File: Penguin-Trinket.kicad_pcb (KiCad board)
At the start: 2 copper layers, 66.3 x 76.5 mm, 17 parts, among them M1 Motor_DC, Q1 NPN, Q2 NPN, Q3 NPN, SW1 SW_Push

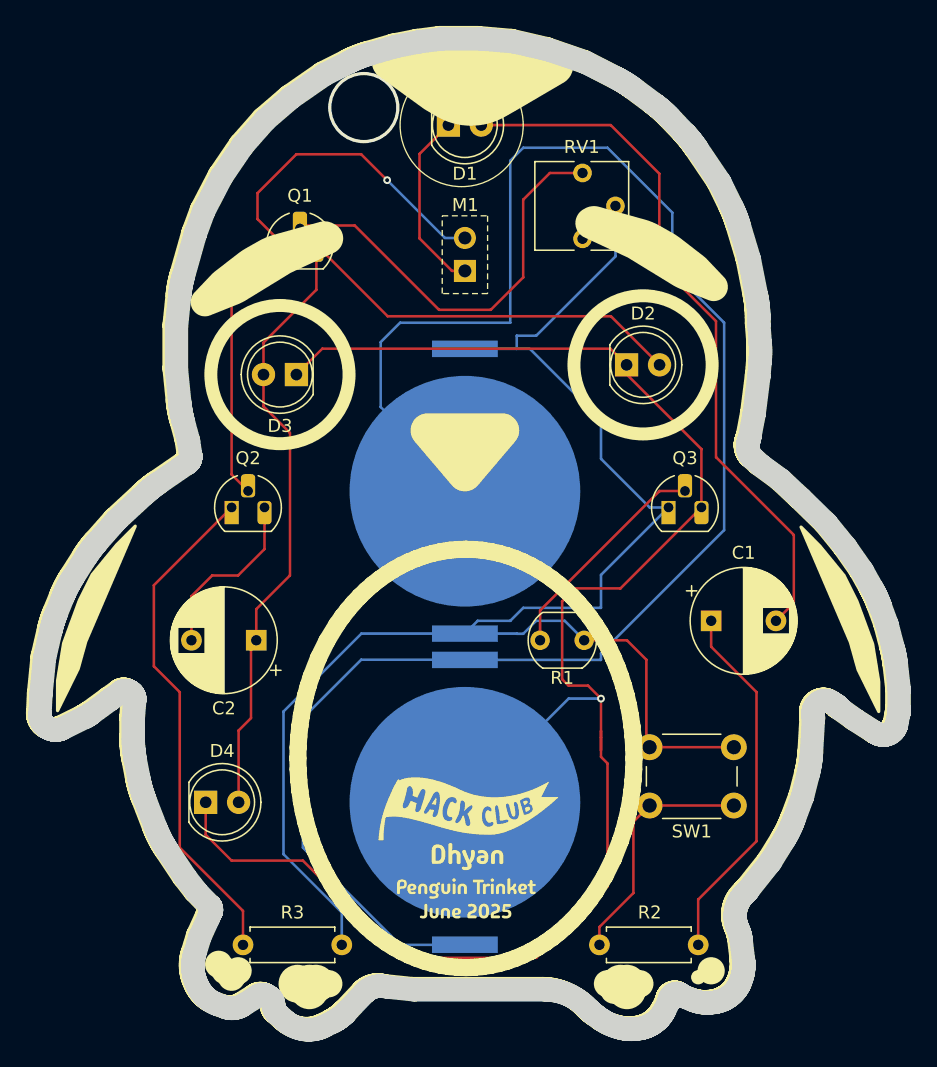
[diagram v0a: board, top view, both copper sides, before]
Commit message: redo (trinket v3)
hopefully everything works
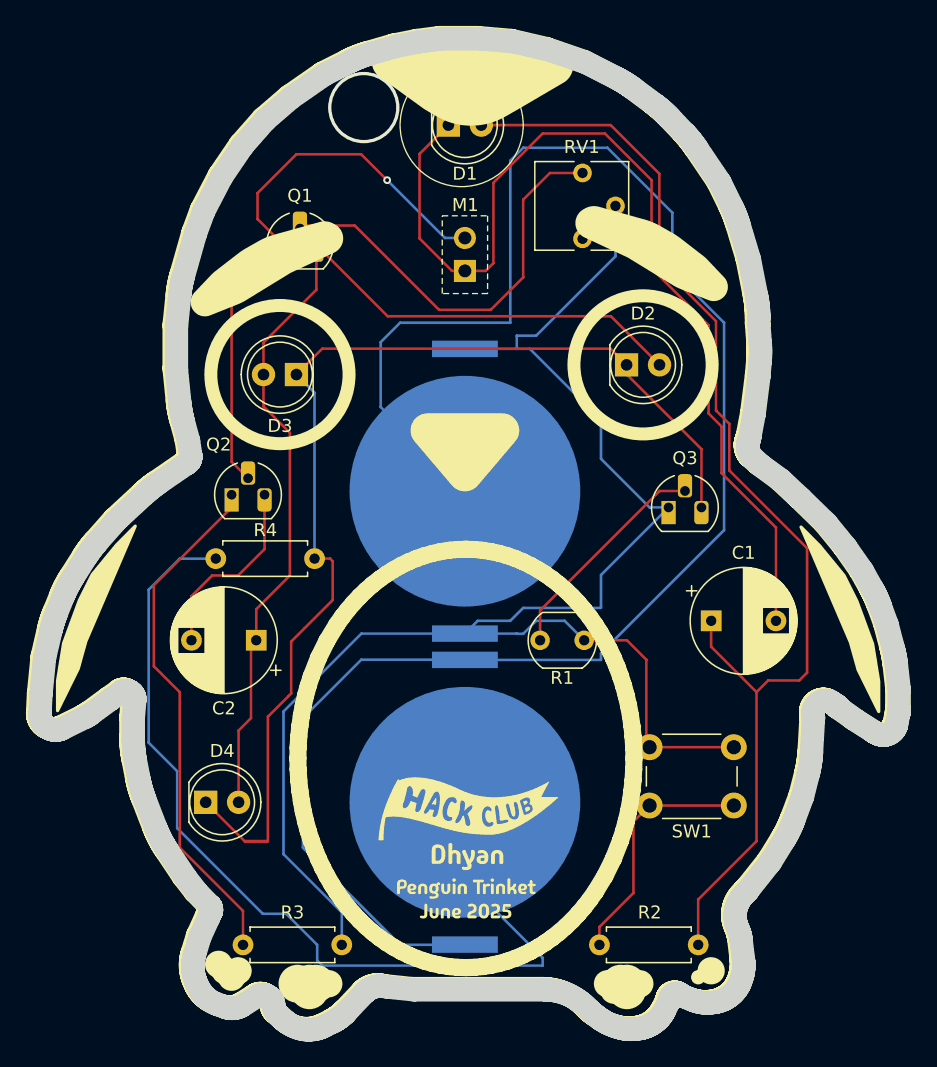
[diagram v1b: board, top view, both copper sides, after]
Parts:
- added R4: R, Resistor_THT:R_Axial_DIN0207_L6.3mm_D2.5mm_P7.62mm_Horizontal, F.Cu at (81.8, 90.2)
- moved Q2 0.98 mm to (83.0, 85.3)
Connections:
- C1 pad 1: Net-(C1-Pad1) -> Net-(D1-A)
- C1 pad 2: Net-(D1-A) -> Net-(D1-K)
- D2 pad 1: GND -> Net-(D2-K)
- D3 pad 1: GND -> Net-(D2-K)
- D4 pad 1: GND -> Net-(D2-K)
- Q3 pad 3: GND -> Net-(D2-K)
- R2 pad 1: Net-(C1-Pad1) -> Net-(D1-A)
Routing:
- net Net-(D2-K): track 0.00 -> 88.0 mm
- net Net-(D1-K): track 14.2 -> 76.1 mm
- net GND: track 134.4 -> 73.9 mm, vias 1 -> 0
- net Net-(D1-A): track 54.7 -> 89.3 mm
- net Net-(C1-Pad1): track 28.3 -> 0.00 mm
- net Net-(Q2-E): track 13.8 -> 14.7 mm
- net Net-(Q2-C): track 39.1 -> 40.1 mm
- net Net-(M1--): track 45.9 -> 44.9 mm
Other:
- board text added: "10µF"
- board text added: "220Ω"
- board text added: "3.0v"
- board text added: "4.7kΩ"
- board text added: "R4"
